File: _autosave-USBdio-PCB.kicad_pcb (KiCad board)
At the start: 2 copper layers, 201.3 x 72.4 mm, 71 parts, among them P0 TE_RELAY_(ORWH-SH-112D), P1 TE_RELAY_(ORWH-SH-112D), P2 TE_RELAY_(ORWH-SH-112D), P3 TE_RELAY_(ORWH-SH-112D), P4 TE_RELAY_(ORWH-SH-112D), P5 TE_RELAY_(ORWH-SH-112D), P6 TE_RELAY_(ORWH-SH-112D), P7 TE_RELAY_(ORWH-SH-112D), Q1 Q_NPN_EBC, Q10 Q_NPN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

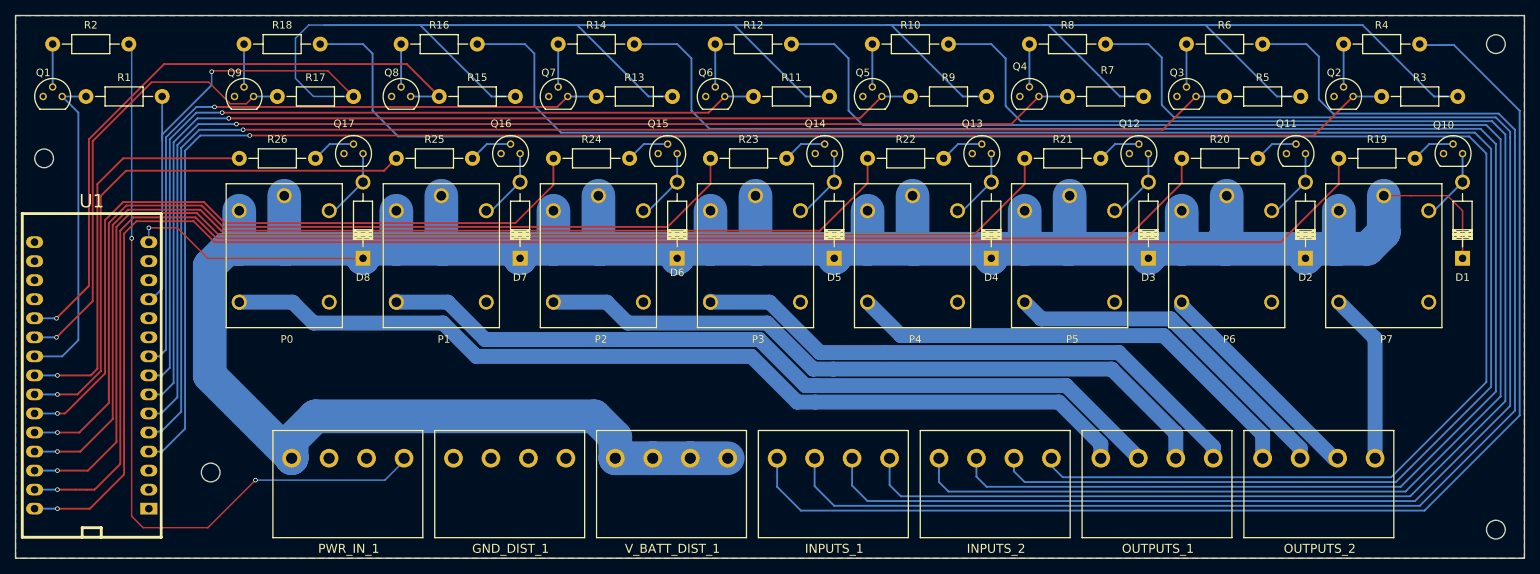
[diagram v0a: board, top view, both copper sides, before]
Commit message: bigger pads for transistors and vias
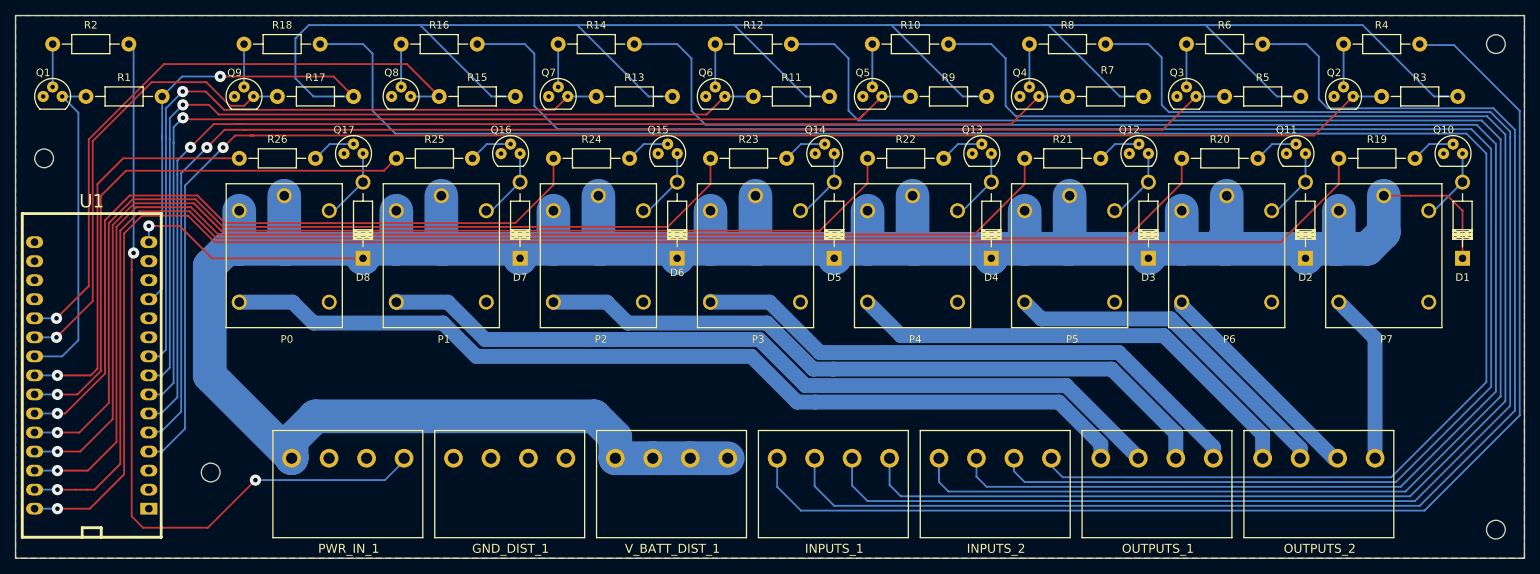
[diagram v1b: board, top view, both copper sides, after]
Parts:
- Q1, Q10, Q11, Q12, Q13, Q14, Q15, Q16, Q17, Q2, Q3, Q4, Q5, Q6, Q7, Q8, Q9: footprint TO_SOT_Packages_THT:TO-92_Molded_Narrow -> USBdio-PCB:TO-92_big_pads
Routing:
- net Net-(Q7-Pad3): track 90.6 -> 94.9 mm
- net Net-(R1-Pad2): track 336.5 -> 332.8 mm
- net Net-(Q6-Pad3): track 113.9 -> 116.7 mm
- net Net-(Q5-Pad3): track 136.9 -> 139.2 mm
- net Net-(Q2-Pad3): track 205.8 -> 203.6 mm
- net Net-(Q3-Pad3): track 182.7 -> 181.2 mm
- net Net-(R24-Pad2): track 99.7 -> 100.4 mm
- net Net-(R22-Pad2): track 146.8 -> 147.5 mm
- net Net-(R23-Pad2): track 123.8 -> 124.4 mm
- net Net-(R20-Pad2): track 193.8 -> 194.5 mm
- net Net-(R21-Pad2): track 170.5 -> 171.2 mm
- net Net-(R19-Pad2): track 216.5 -> 217.1 mm
- net Net-(PWR_IN_1-Pad4): track 104.2 -> 104.7 mm
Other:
- net class 5 Amps: via_dia 0.6 -> 1.5; via_drill 0.4 -> 0.6
- net class Default: via_dia 0.6 -> 1.5; via_drill 0.4 -> 0.6
- net class High Amps: via_dia 0.6 -> 1.5; via_drill 0.4 -> 0.6
